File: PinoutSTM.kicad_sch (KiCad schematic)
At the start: 12 parts, among them IC1 STM32H7B0RBT6, J4 1761681-3, J6 Header male 1x05, SW1 Button Switch SPST-No, Y1 CC4V-T1A-32.768kHz-6pF-20PPM-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

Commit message: resolve project breaking merge conflict miss
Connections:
- net +3.3V: now also R8.2
- net 3V3_ext: now also R10.2
- net CAN1_RX: now also IC1.43 (PA11)
- net CAN1_TX: now also IC1.44 (PA12)
- net GND: now also C1.2, IC1.12 (VSSA), IC1.18 (VSS_1), IC1.31 (VSS_2), IC1.47 (VSS_3), IC1.63 (VSS_4), J4.5 (GND), J4.6 (GND)
- net JTAG_ TDI: now also IC1.50 (PA15)
- net JTAG_TCK/SWCLK: now also IC1.49 (PA14), J4.2 (SWCLK)
- net JTAG_TDO/SWO: now also IC1.55 (PB3), J4.3 (SWIM)
- net JTAG_TMS/SWDIO: now also IC1.45 (PA13), J4.4 (SWDIO)
- net SPI1_MISO: now also IC1.22 (PA6)
- net SPI1_MOSI: now also IC1.23 (PA7)
- net SPI1_NSS: now also IC1.20 (PA4)
- net SPI1_SCK: now also IC1.21 (PA5)
- net STM_BOOT0: now also IC1.60 (BOOT0)
- net STM_USART_RX: now also IC1.17 (PA3)
- net STM_USART_TX: now also IC1.16 (PA2)
- net USART1_RX: now also IC1.42 (PA10)
- net USART1_TX: now also IC1.41 (PA9)
- net Vdd: now also IC1.1 (VBAT), IC1.13 (VDDA), IC1.19 (VDD_1), IC1.32 (VDD_2), IC1.48 (VDD_3), IC1.64 (VDD_4), J4.7 (3V3), J4.8 (3V3), R10.1, R8.1
- net nRST: now also J4.1 (~{RST})
- net at C2.1, Y1.1: now also IC1.4 (PC15-OSC32_OUT)
- net at C1.1, Y1.2 (OUTPUT): now also IC1.3 (PC14-OSC32_IN)
- net at C3.1: now also IC1.30 (VCAP_1)
- net at C4.1: now also IC1.46 (VCAP_2)
- new net: J4.10 (5V), J4.9 (5V)
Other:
- moved on the sheet: C1, C2, C3, C4, IC1, Y1

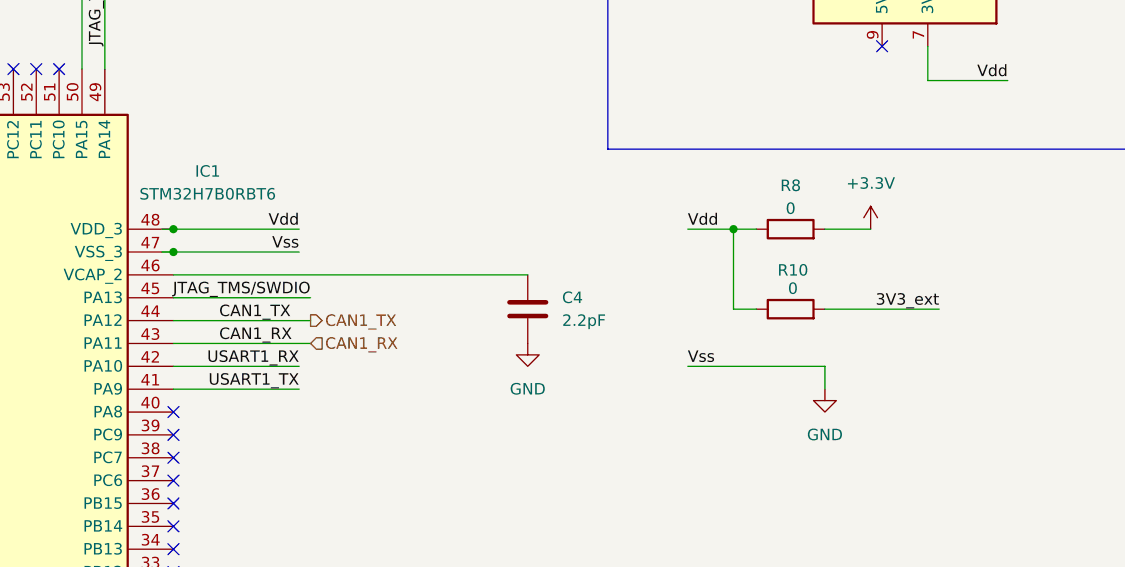
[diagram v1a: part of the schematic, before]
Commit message: CAN tranciever
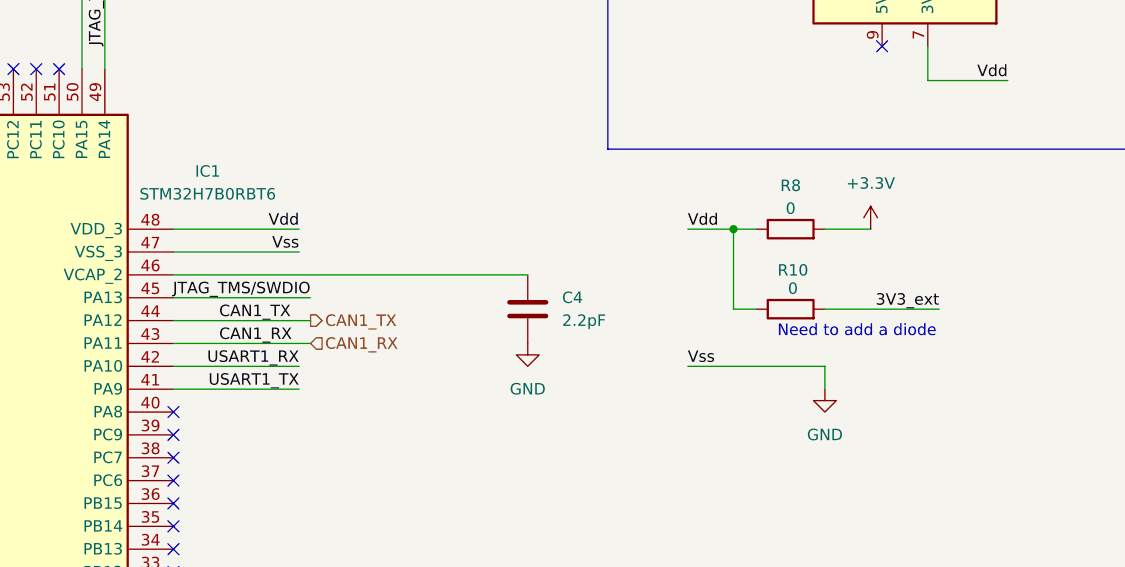
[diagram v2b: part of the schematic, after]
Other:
- note added: "Need to add a diode"
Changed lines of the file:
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@@
 	(generator_version "9.0")
 	(paper "A4")
+	(text "Need to add a diode\n"
+		(exclude_from_sim no)
+		(at 201.676 83.82 0)
+		(effects
+			(font
+				(size 1.27 1.27)
+			)
+		)
+	)
 	(text "External interfaces\n\n"
 		(exclude_from_sim no)
@@
 	)
 	(junction
-		(at 125.73 72.39)
-		(diameter 0)
-		(color 0 0 0 0)
-	)
-	(junction
 		(at 251.46 44.45)
 		(diameter 0)
@@
 		(color 0 0 0 0)
 	)
-	(junction
-		(at 125.73 74.93)
-		(diameter 0)
-		(color 0 0 0 0)
-	)
 	(no_connect
 		(at 92.71 54.61)
@@
 	(wire
 		(pts
-			(xy 124.46 74.93) (xy 125.73 74.93)
-		)
-		(stroke
-			(width 0)
-			(type default)
-		)
-	)
-	(wire
-		(pts
-			(xy 124.46 72.39) (xy 125.73 72.39)
-		)
-		(stroke
-			(width 0)
-			(type default)
-		)
-	)
-	(wire
-		(pts
 			(xy 266.7 53.34) (xy 266.7 54.61)
 		)
@@
 	(wire
 		(pts
+			(xy 223.52 17.78) (xy 223.52 21.59)
+		)
+		(stroke
+			(width 0)
+			(type default)
+		)
+	)
+	(wire
+		(pts
+			(xy 85.09 128.27) (xy 85.09 139.7)
+		)
+		(stroke
+			(width 0)
+			(type default)
+		)
+	)
+	(wire
+		(pts
+			(xy 50.8 86.36) (xy 53.34 86.36)
+		)
+		(stroke
+			(width 0)
+			(type default)
+		)
+	)
+	(wire
+		(pts
+			(xy 118.11 36.83) (xy 118.11 54.61)
+		)
+		(stroke
+			(width 0)
+			(type default)
+		)
+	)
+	(wire
+		(pts
+			(xy 251.46 27.94) (xy 259.08 27.94)
+		)
+		(stroke
+			(width 0)
+			(type default)
+		)
+	)
+	(wire
+		(pts
 			(xy 125.73 72.39) (xy 139.7 72.39)
 		)
@@
 	(wire
 		(pts
-			(xy 223.52 17.78) (xy 223.52 21.59)
-		)
-		(stroke
-			(width 0)
-			(type default)
-		)
-	)
-	(wire
-		(pts
-			(xy 85.09 128.27) (xy 85.09 139.7)
-		)
-		(stroke
-			(width 0)
-			(type default)
-		)
-	)
-	(wire
-		(pts
-			(xy 50.8 86.36) (xy 53.34 86.36)
-		)
-		(stroke
-			(width 0)
-			(type default)
-		)
-	)
-	(wire
-		(pts
-			(xy 118.11 36.83) (xy 118.11 54.61)
-		)
-		(stroke
-			(width 0)
-			(type default)
-		)
-	)
-	(wire
-		(pts
-			(xy 251.46 27.94) (xy 259.08 27.94)
-		)
-		(stroke
-			(width 0)
-			(type default)
-		)
-	)
-	(wire
-		(pts
 			(xy 90.17 36.83) (xy 90.17 54.61)
 		)
@@
 	(wire
 		(pts
+			(xy 125.73 74.93) (xy 139.7 74.93)
+		)
+		(stroke
+			(width 0)
+			(type default)
+		)
+	)
+	(wire
+		(pts
 			(xy 182.88 72.39) (xy 187.96 72.39)
 		)
@@
 		)
 		(stroke
-			(width 0)
-			(type default)
-		)
-	)
-	(wire
-		(pts
-			(xy 125.73 74.93) (xy 139.7 74.93)
-		)
-		(stroke

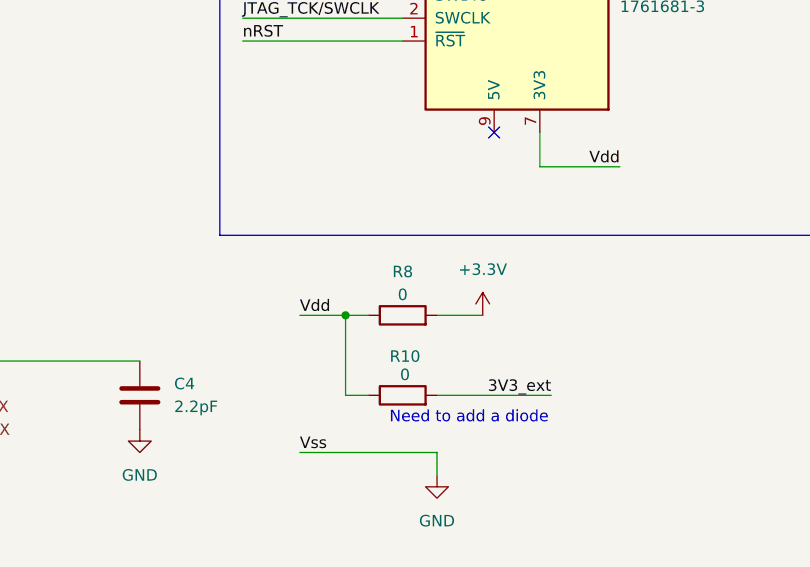
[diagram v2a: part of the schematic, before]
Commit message: multiple changes. fixed some mistakes, added jumper pins for wifi
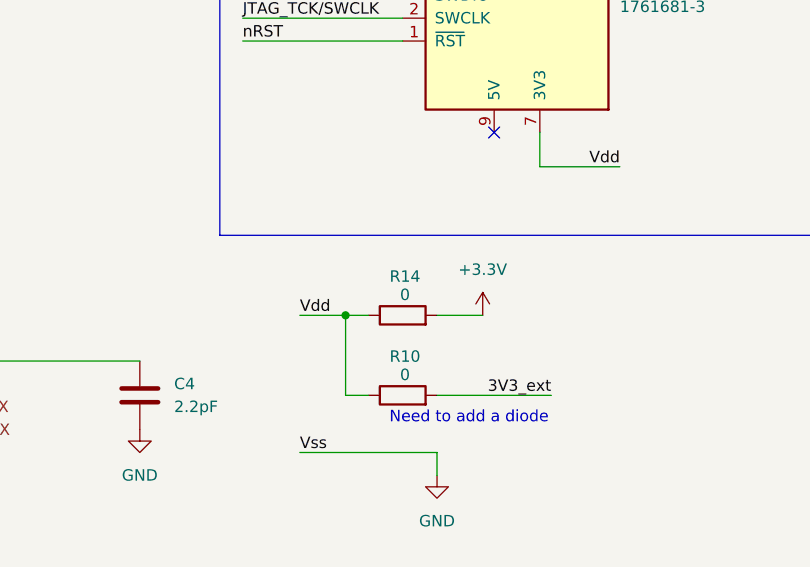
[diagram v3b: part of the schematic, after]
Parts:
- removed R8: 0, Resistor_SMD:R_0603_1608Metric, symbol #dzdb:g_res/R-0-0603
- added R14: 0, Resistor_SMD:R_0603_1608Metric, symbol #dzdb:g_res/R-0-0603
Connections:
- net +3.3V: now also R14.2
- net Vdd: now also R14.1
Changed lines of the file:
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@@
+	)
+	(symbol
+		(lib_id "#dzdb:g_res/R-0-0603")
+		(at 194.31 72.39 90)
+		(unit 1)
+		(exclude_from_sim no)
+		(in_bom yes)
+		(on_board yes)
+		(dnp no)
+		(property "Reference" "R14"
+			(at 194.564 68.072 90)
+			(effects
+				(font
+					(size 1.27 1.27)
+				)
+			)
+		)
+		(property "Value" "0"
+			(at 194.564 70.104 90)
+			(effects
+				(font
+					(size 1.27 1.27)
+				)
+			)
+		)
+		(property "Footprint" "Resistor_SMD:R_0603_1608Metric"
+			(at 194.31 74.168 90)
+			(effects
+				(font
+					(size 1.27 1.27)
+				)
+				(hide yes)
+			)
+		)
+		(property "Datasheet" "https://www.we-online.com/components/products/datasheet/560112116001.pdf"
+			(at 194.31 72.39 0)
+			(effects
+				(font
+					(size 1.27 1.27)
+				)
+				(hide yes)
+			)
+		)
+		(property "Description" "Thick Film Resistors - SMD WRIS-RSKS <0.05 Ohms  0.1 W Jumper 0603"
+			(at 194.31 72.39 0)
+			(effects
+				(font
+					(size 1.27 1.27)
+				)
+				(hide yes)
+			)
+		)
+		(property "IPN" "R-0-0603"
+			(at 194.31 72.39 0)
+			(effects
+				(font
+					(size 1.27 1.27)
+				)
+				(hide yes)
+			)
+		)
+		(property "MPN" "560112116001"
+			(at 194.31 72.39 0)
+			(effects
+				(font
+					(size 1.27 1.27)
+				)
+				(hide yes)
+			)
+		)
+		(property "Manufacturer" "Wurth Elektronik"
+			(at 194.31 72.39 0)
+			(effects
+				(font
+					(size 1.27 1.27)
+				)
+				(hide yes)
+			)
+		)
+		(property "Resistance" "0"
+			(at 194.31 72.39 0)
+			(effects
+				(font
+					(size 1.27 1.27)
+				)
+				(hide yes)
+			)
+		)
+		(property "Power" "0.1W"
+			(at 194.31 72.39 0)
+			(effects
+				(font
+					(size 1.27 1.27)
+				)
+				(hide yes)
+			)
+		)
+		(property "Material" "Thick film"
+			(at 194.31 72.39 0)
+			(effects
+				(font
+					(size 1.27 1.27)
+				)
+				(hide yes)
+			)
+		)
+		(property "Tolerance" "5%"
+			(at 194.31 72.39 0)
+			(effects
+				(font
+					(size 1.27 1.27)
+				)
+				(hide yes)
+			)
+		)
+		(property "Supplier" "Mouser"
+			(at 194.31 72.39 0)
+			(effects
+				(font
+					(size 1.27 1.27)
+				)
+				(hide yes)
+			)
+		)
+		(property "SPN" "710-560112116001"
+			(at 194.31 72.39 0)
+			(effects
+				(font
+					(size 1.27 1.27)
+				)
+				(hide yes)
+			)
+		)
+		(property "LCSC" "CXXXXX"
+			(at 194.31 72.39 0)
+			(effects
+				(font
+					(size 1.27 1.27)
+				)
+				(hide yes)
+			)
+		)
+		(property "Comment" "lifecycle=Active; note=Auto-generated"
+			(at 194.31 72.39 0)
+			(effects
+				(font
+					(size 1.27 1.27)
+				)
+				(hide yes)
+			)
+		)
+		(pin "2"
+		)
+		(pin "1"
+		)
+		(instances
+			(project "nautilus_mainboard"
+				(path "/ce1819b2-f280-40ed-834f-6fe4d12f809d/46fb4fb5-44f2-465b-b1ff-e4e0fbef74ae/fadabe7f-e4de-4ec7-8fb6-d9f38e9db4fc"
+					(reference "R14")
+					(unit 1)
+				)
+			)
+		)
 	)
 	(symbol
@@
 					(unit 1)
 				)
-			)
-		)
-	)
-	(symbol
-		(lib_id "#dzdb:g_res/R-0-0603")
-		(at 194.31 72.39 90)
-		(unit 1)
-		(exclude_from_sim no)
-		(in_bom yes)
-		(on_board yes)
-		(dnp no)
-		(property "Reference" "R8"
-			(at 194.31 67.564 90)
-			(effects
-				(font
-					(size 1.27 1.27)
-				)
-			)
-		)
-		(property "Value" "0"
-			(at 194.31 70.104 90)
-			(effects
-				(font
-					(size 1.27 1.27)
-				)
-			)
-		)
-		(property "Footprint" "Resistor_SMD:R_0603_1608Metric"
-			(at 194.31 74.168 90)
-			(effects
-				(font
-					(size 1.27 1.27)
-				)
-				(hide yes)
-			)
-		)
-		(property "Datasheet" "https://www.we-online.com/components/products/datasheet/560112116001.pdf"
-			(at 194.31 72.39 0)
-			(effects
-				(font
-					(size 1.27 1.27)
-				)
-				(hide yes)
-			)
-		)
-		(property "Description" "Thick Film Resistors - SMD WRIS-RSKS <0.05 Ohms  0.1 W Jumper 0603"
-			(at 194.31 72.39 0)
-			(effects
-				(font
-					(size 1.27 1.27)
-				)
-				(hide yes)
-			)
-		)
-		(property "IPN" "R-0-0603"
-			(at 194.31 72.39 0)
-			(effects
-				(font
-					(size 1.27 1.27)
-				)
-				(hide yes)
-			)
-		)
-		(property "MPN" "560112116001"
-			(at 194.31 72.39 0)
-			(effects
-				(font
-					(size 1.27 1.27)
-				)
-				(hide yes)
-			)
-		)
-		(property "Manufacturer" "Wurth Elektronik"
-			(at 194.31 72.39 0)
-			(effects
-				(font
-					(size 1.27 1.27)
-				)
-				(hide yes)
-			)
-		)
-		(property "Resistance" "0"
-			(at 194.31 72.39 0)
-			(effects
-				(font
-					(size 1.27 1.27)
-				)
-				(hide yes)
-			)
-		)
-		(property "Power" "0.1W"
-			(at 194.31 72.39 0)
-			(effects
-				(font
-					(size 1.27 1.27)
-				)
-				(hide yes)
-			)
-		)
-		(property "Material" "Thick film"
-			(at 194.31 72.39 0)
-			(effects
-				(font
-					(size 1.27 1.27)
-				)
-				(hide yes)
-			)
-		)
-		(property "Tolerance" "5%"
-			(at 194.31 72.39 0)
-			(effects
-				(font
-					(size 1.27 1.27)
-				)
-				(hide yes)
-			)
-		)
-		(property "Supplier" "Mouser"
-			(at 194.31 72.39 0)
-			(effects
-				(font
-					(size 1.27 1.27)
-				)
-				(hide yes)
-			)
-		)
-		(property "SPN" "710-560112116001"
-			(at 194.31 72.39 0)
-			(effects
-				(font
-					(size 1.27 1.27)
-				)
-				(hide yes)
-			)
-		)
-		(property "LCSC" "CXXXXX"
-			(at 194.31 72.39 0)
-			(effects
-				(font
-					(size 1.27 1.27)
-				)
-				(hide yes)
-			)
-		)
-		(property "Comment" "lifecycle=Active; note=Auto-generated"
-			(at 194.31 72.39 0)
-			(effects
-				(font
-					(size 1.27 1.27)
-				)
-				(hide yes)
-			)
-		)
-		(pin "2"
-		)
-		(pin "1"
-		)
-		(instances
-			(project ""
-				(path "/ce1819b2-f280-40ed-834f-6fe4d12f809d/46fb4fb5-44f2-465b-b1ff-e4e0fbef74ae/fadabe7f-e4de-4ec7-8fb6-d9f38e9db4fc"
-					(reference "R8")
-					(unit 1)
-				)

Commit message: added caps
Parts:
- added C13: 100nF, Capacitor_SMD:C_0603_1608Metric, symbol #dzdb:g_cap/C-100n-0603
- added C14, C15, C16, C17, C18, C19: 10pF, Capacitor_SMD:C_0603_1608Metric, symbol #dzdb:g_cap/C-10p-0603
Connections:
- net BOOT0 is gone; now on net STM_BOOT0: J6.4 (Pin_4)
- net GND: now also C13.2, C14.2, C15.2, C16.2, C17.2, C18.2, C19.2
- net Vdd: now also C13.1, C14.1, C15.1, C16.1, C17.1, C18.1, C19.1

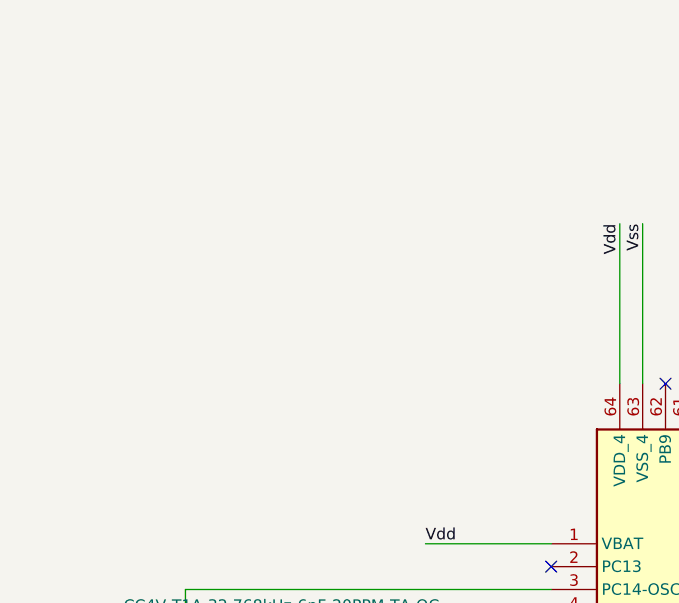
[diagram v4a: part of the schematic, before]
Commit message: added fan Mosfet
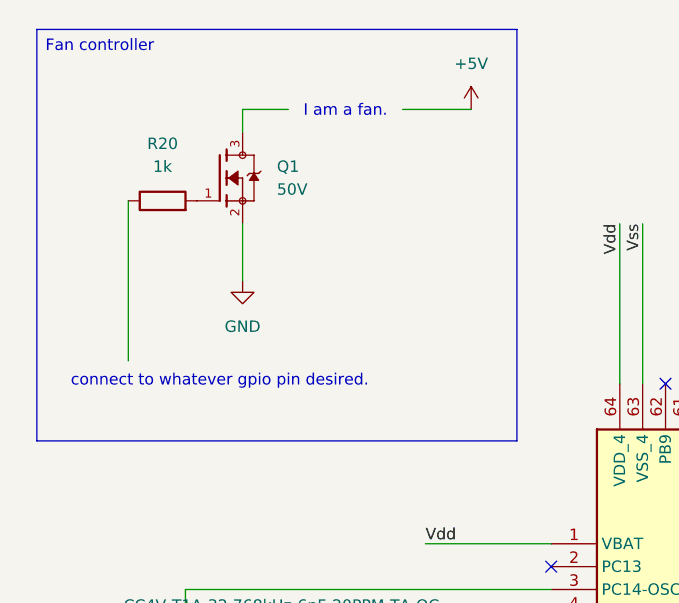
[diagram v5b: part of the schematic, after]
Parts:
- added Q1: 50V, dz_dio:onsemi_Mosfet_BSS138, symbol #dzdb:s_misc/ONSE-BSS138
- added R20: 1k, Resistor_SMD:R_0603_1608Metric, symbol #dzdb:g_res/R-1k-0603
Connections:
- net GND: now also Q1.2
- new net: Q1.1, R20.2
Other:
- note added: "I am a fan."
- note added: "connect to whatever gpio pin desired."

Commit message: Added Power logic finally. (plus some comments on further improvements)
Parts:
- removed R10, R14: 0, Resistor_SMD:R_0603_1608Metric, symbol #dzdb:g_res/R-0-0603
- added J2: 61300211121, dz_con:Wurth_Con_61300211121, symbol #dzdb:s_con/WURT-61300211121
- added R4: 0, Resistor_SMD:R_0603_1608Metric, symbol #dzdb:g_res/R-0-0603
- renumbered C3 to C10, C13 to C11, C14 to C12, C15 to C13, C16 to C14, C4 to C15, C17 to C16, C18 to C17, C19 to C18, C6 to C19, C1 to C8, C2 to C9, J4 to J3, J6 to J4, R20 to R3
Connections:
- net 3V3_ext: no longer J4.1 (Pin_1)
- net GND: now also J2.2
- net Vdd renamed STM_IN_3.3V
- new net: J2.1, R4.2
- new net Battery_Out_5V: R4.1
- new net STM_Plug_3.3V: J4.1 (Pin_1)
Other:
- note added: "- +"
- note added: "3v3 ext was first implemented here"
- note added: "fan only active when battery is connected. Mby add an external power pin to externally power the fan for testing."
- note added: "logic handled in power section"
- note removed: "Need to add a diode"

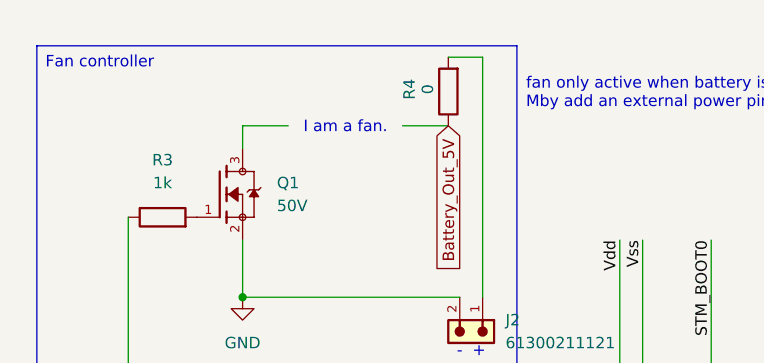
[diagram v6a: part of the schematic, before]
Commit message: added Gyroscope and Accelerometer part (4x) over IIC
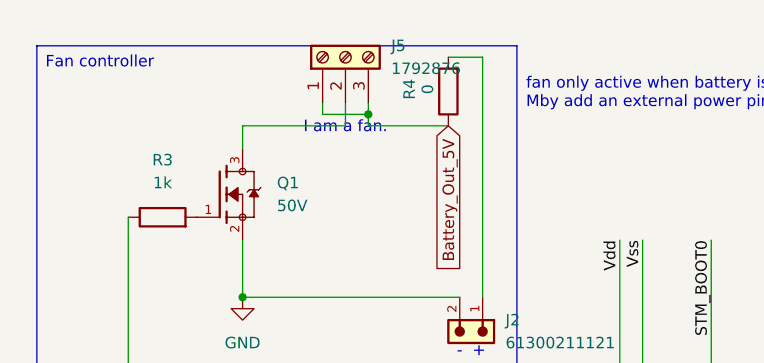
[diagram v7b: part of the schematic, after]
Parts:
- added J5: 1792876, TerminalBlock_Phoenix:TerminalBlock_Phoenix_PT-1,5-3-5.0-H_1x03_P5.00mm_Horizontal, symbol #dzdb:s_con/CON-PHO-1792876
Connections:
- net Battery_Out_5V: now also J5.1 (Pin_1), J5.3 (Pin_3)
- net at Q1.3: now also J5.2 (Pin_2)
